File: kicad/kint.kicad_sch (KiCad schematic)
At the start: 25 parts, among them J1 THUMB_RIGHT_SPC_KB600, J2 LEFT_13_LT, J3 TOP_LEFT, J4 TOP_RIGHT, J5 THUMB_LEFT_BAK, J6 THUMB_RIGHT_SPC, J7 RIGHT_13_DOWN, J8 THUMB_LEFT_BAK_KB600, U1 TEENSY_3.5_3.6

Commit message: v1.0.0
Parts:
- removed JP4, JP5, JP6: SolderJumper_2_Bridged, Jumper:SolderJumper-2_P1.3mm_Bridged2Bar_RoundedPad1.0x1.5mm, symbol Jumper:SolderJumper_2_Bridged
- removed U1: TEENSY_3.5_3.6, kinx:TEENSY_3.5_3.6, symbol kinx-eagle-import:TEENSY_3.5_3.6
- added A1: Feather_ItsyBitsy_ProMicro_MCU, kinx:Feather_Teensy_ProMicro, symbol kintqt:Feather_ItsyBitsy_ProMicro_MCU
- added J10: Conn_01x09, Connector_PinHeader_2.54mm:PinHeader_1x09_P2.54mm_Vertical, symbol Connector_Generic:Conn_01x09
- added J11: USB_A, Connector_PinHeader_2.54mm:PinHeader_1x05_P2.54mm_Vertical, symbol Connector:USB_A
- added J12: Conn_StemmaQT, Connector_PinHeader_2.54mm:PinHeader_1x04_P2.54mm_Vertical, symbol Connector_Generic:Conn_01x04
- added J9: Conn_01x09_Male, Connector_JST:JST_PH_B9B-PH-K_1x09_P2.00mm_Vertical, symbol kintqt:Conn_01x09_Male
- added JP10, JP11, JP4, JP5, JP6, JP7, JP8, JP9: SolderJumper_2_Open, Jumper:SolderJumper-2_P1.3mm_Open_TrianglePad1.0x1.5mm, symbol Jumper:SolderJumper_2_Open
- added R5, R6: 4.7K, Resistor_SMD:R_1206_3216Metric_Pad1.30x1.75mm_HandSolder, symbol Device:R
- added U2, U3: MCP23017_SP, Package_DIP:DIP-28_W7.62mm, symbol Interface_Expansion:MCP23017_SP
- JP1, JP2, JP3: footprint Jumper:SolderJumper-2_P1.3mm_Open_RoundedPad1.0x1.5mm -> Jumper:SolderJumper-2_P1.3mm_Open_TrianglePad1.0x1.5mm
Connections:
- net COL_0: now also U2.21 (GPA0)
- net COL_1: now also U2.22 (GPA1)
- net COL_2: now also U2.23 (GPA2); no longer JP3.2 (B)
- net COL_3: now also U2.24 (GPA3)
- net COL_4: now also U2.25 (GPA4)
- net COL_5: now also U2.26 (GPA5)
- net COL_6: now also U2.27 (GPA6)
- net GND: now also A1.4 (GND), J10.4 (Pin_4), J11.4 (GND), J12.4 (Pin_4), J9.4 (Pin_4), JP4.1 (A), U2.10 (VSS), U2.16 (A1), U2.17 (A2), U3.10 (VSS), U3.15 (A0), U3.16 (A1), U3.17 (A2)
- net LED_CAPS_LOCK: now also U2.7 (GPB6)
- net LED_KEYPAD: now also U2.8 (GPB7)
- net LED_NUM_LOCK: now also U2.28 (GPA7)
- net LED_SCROLL_LOCK: now also U3.8 (GPB7)
- net ROW_0: now also U3.3 (GPB2)
- net ROW_1: now also U3.22 (GPA1)
- net ROW_2: now also U3.23 (GPA2)
- net ROW_3: now also U3.24 (GPA3)
- net ROW_4: now also U3.25 (GPA4); no longer JP1.2 (B)
- net ROW_5: now also U3.26 (GPA5); no longer JP2.2 (B)
- net ROW_6: now also U3.27 (GPA6)
- net ROW_7: now also U3.28 (GPA7)
- net ROW_8: now also U3.1 (GPB0)
- net ROW_9: now also U3.2 (GPB1)
- net ROW_EQL: now also U3.21 (GPA0)
- net ROW_ESC: now also U3.5 (GPB4)
- net ROW_F1: now also U3.6 (GPB5)
- net ROW_F2: now also U3.7 (GPB6)
- net ROW_MIN: now also U3.4 (GPB3)
- net VBUS: now reaches JP1.1 (A)
- net VBUS: now also J10.1 (Pin_1), J11.1 (VBUS), J9.1 (Pin_1), JP11.1 (A)
- net D-: now reaches JP2.1 (A)
- net D-: now also J10.3 (Pin_3), J11.2 (D-), J9.3 (Pin_3)
- net D+: now reaches JP3.1 (A)
- net D+: now also J10.2 (Pin_2), J11.3 (D+), J9.2 (Pin_2)
- net 3V3 renamed +3.3V
- net +3.3V: now also A1.2 (3V3), J12.3 (Pin_3), JP7.1 (A), R5.1, R6.2, U2.15 (A0), U2.18 (~{RESET}), U2.9 (VDD), U3.18 (~{RESET}), U3.9 (VDD)
- new net: J10.6 (Pin_6), J9.6 (Pin_6)
- new net: J10.7 (Pin_7), J9.7 (Pin_7)
- new net: J10.8 (Pin_8), J9.8 (Pin_8)
- new net: J10.9 (Pin_9), J9.9 (Pin_9)
- new net F_SCL: A1.18 (SCL), JP9.2 (B)
- new net F_SDA: A1.17 (SDA), JP10.2 (B)
- new net F_USB: A1.26 (USB), JP11.2 (B)
- new net K_3V3: A1.24 (D5), JP7.2 (B)
- new net K_DM: A1.28 (VBAT), JP2.2 (B)
- new net K_DP: A1.5 (A0), JP3.2 (B)
- new net K_GND: A1.9 (A4), JP4.2 (B)
- new net K_RESET: A1.25 (D6), JP8.2 (B)
- new net K_SCL: A1.11 (SCK), JP5.2 (B)
- new net K_SDA: A1.10 (A5), JP6.2 (B)
- new net K_USB: A1.27 (EN), JP1.2 (B)
- new net RESET: A1.1 (~{RESET}), JP8.1 (A)
- new net SCL: J12.1 (Pin_1), JP5.1 (A), JP9.1 (A), R5.2, U2.12 (SCK), U3.12 (SCK)
- new net SDA: J12.2 (Pin_2), JP10.1 (A), JP6.1 (A), R6.1, U2.13 (SDA), U3.13 (SDA)
- new net SHIELD: J10.5 (Pin_5), J9.5 (Pin_5)
- no-connect marks 52 -> 56
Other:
- note removed: "TEENSY_POWER_LED"
- note removed: "Teensy++"
- note removed: "only present on: Teensy 3.5 Teensy 3.6 Teensy 4.1"
- moved on the sheet: LED1, LED2, LED3, LED4, R1, R2, R3, R4

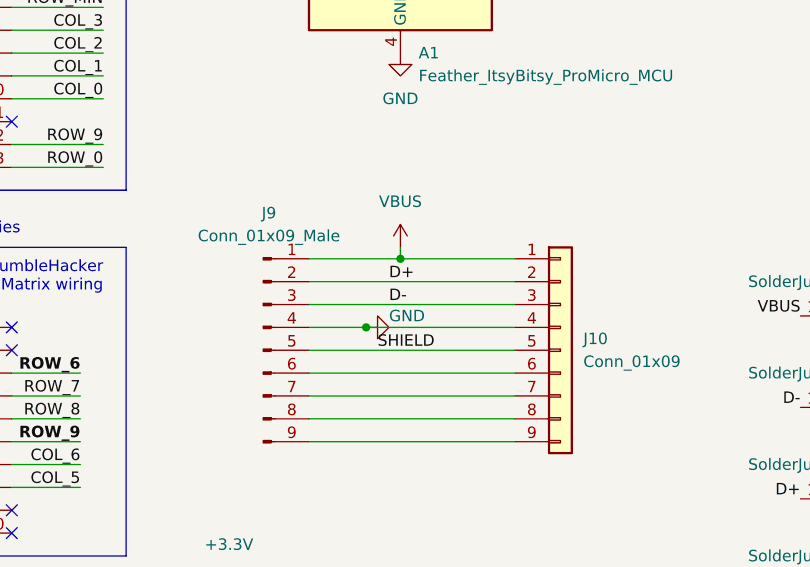
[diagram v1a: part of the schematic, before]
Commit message: fixing routing for D+ and D-
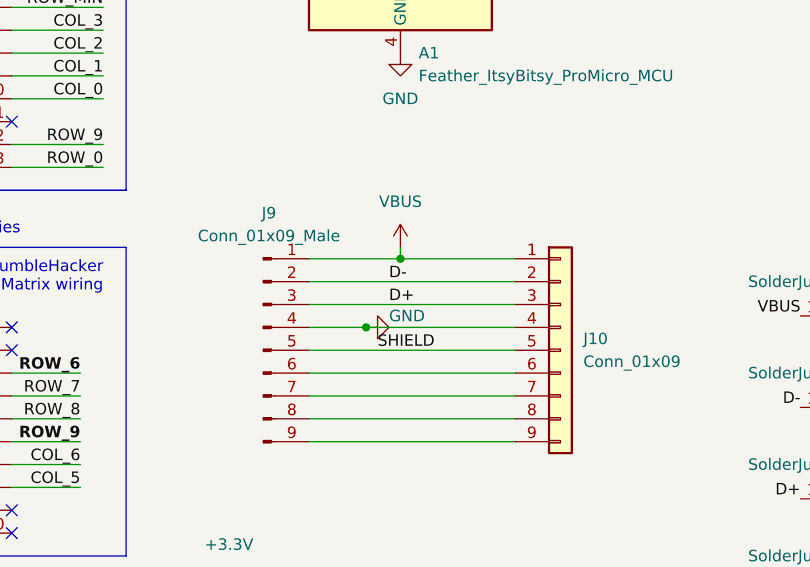
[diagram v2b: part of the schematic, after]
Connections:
- net D+: now also J10.3 (Pin_3), J9.3 (Pin_3); no longer J10.2 (Pin_2), J9.2 (Pin_2)
- net D-: now also J10.2 (Pin_2), J9.2 (Pin_2); no longer J10.3 (Pin_3), J9.3 (Pin_3)
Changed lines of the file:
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@@
     (effects (font (size 1.27 1.27)) (justify right bottom))
   )
-  (label "D+" (at 82.55 115.57 0)
+  (label "D-" (at 82.55 115.57 0)
     (effects (font (size 1.27 1.27)) (justify left bottom))
   )
@@
     (effects (font (size 1.27 1.27)) (justify right bottom))
   )
-  (label "D-" (at 82.55 118.11 0)
+  (label "D+" (at 82.55 118.11 0)
     (effects (font (size 1.27 1.27)) (justify left bottom))
   )

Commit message: Updating schematic title and images
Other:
- company: Michael Stapelberg -> Benjamin Gould
- title: kinT keyboard controller -> kinT-QT keyboard controller
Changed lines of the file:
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@@
   (paper "A4")
   (title_block
-    (title "kinT keyboard controller")
+    (title "kinT-QT keyboard controller")
     (date "2021-06-26")
-    (company "Michael Stapelberg")
-    (comment 1 "https://github.com/kinx-project/kint")
+    (company "Benjamin Gould")
+    (comment 1 "https://github.com/bgould/kint-qt")
   )
   (junction (at 158.115 35.56) (diameter 0) (color 0 0 0 0)
